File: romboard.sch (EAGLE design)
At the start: 13 parts

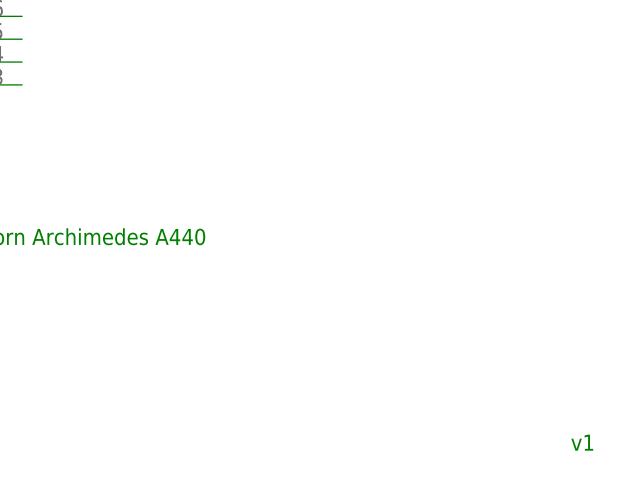
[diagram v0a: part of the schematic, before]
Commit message: Add licence to schematic, board
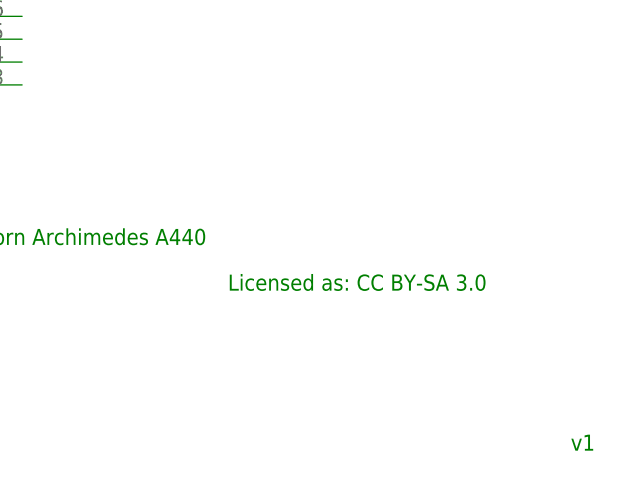
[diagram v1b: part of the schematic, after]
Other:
- note added: "Licensed as: CC BY-SA 3.0"
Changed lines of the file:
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@@
 <grid distance="0.1" unitdist="inch" unit="inch" style="lines" multiple="1" display="no" altdistance="0.01" altunitdist="inch" altunit="inch"/>
 <layers>
-<layer number="1" name="Top" color="4" fill="1" visible="yes" active="no"/>
-<layer number="16" name="Bottom" color="1" fill="1" visible="yes" active="no"/>
-<layer number="17" name="Pads" color="2" fill="1" visible="yes" active="no"/>
-<layer number="18" name="Vias" color="2" fill="1" visible="yes" active="no"/>
-<layer number="19" name="Unrouted" color="6" fill="1" visible="yes" active="no"/>
-<layer number="20" name="Dimension" color="15" fill="1" visible="yes" active="no"/>
-<layer number="21" name="tPlace" color="7" fill="1" visible="yes" active="no"/>
-<layer number="22" name="bPlace" color="7" fill="1" visible="yes" active="no"/>
-<layer number="23" name="tOrigins" color="15" fill="1" visible="yes" active="no"/>
-<layer number="24" name="bOrigins" color="15" fill="1" visible="yes" active="no"/>
-<layer number="25" name="tNames" color="7" fill="1" visible="yes" active="no"/>
-<layer number="26" name="bNames" color="7" fill="1" visible="yes" active="no"/>
-<layer number="27" name="tValues" color="7" fill="1" visible="yes" active="no"/>
-<layer number="28" name="bValues" color="7" fill="1" visible="yes" active="no"/>
+<layer number="1" name="Top" color="4" fill="1" visible="no" active="no"/>
+<layer number="16" name="Bottom" color="1" fill="1" visible="no" active="no"/>
+<layer number="17" name="Pads" color="2" fill="1" visible="no" active="no"/>
+<layer number="18" name="Vias" color="2" fill="1" visible="no" active="no"/>
+<layer number="19" name="Unrouted" color="6" fill="1" visible="no" active="no"/>
+<layer number="20" name="Dimension" color="15" fill="1" visible="no" active="no"/>
+<layer number="21" name="tPlace" color="7" fill="1" visible="no" active="no"/>
+<layer number="22" name="bPlace" color="7" fill="1" visible="no" active="no"/>
+<layer number="23" name="tOrigins" color="15" fill="1" visible="no" active="no"/>
+<layer number="24" name="bOrigins" color="15" fill="1" visible="no" active="no"/>
+<layer number="25" name="tNames" color="7" fill="1" visible="no" active="no"/>
+<layer number="26" name="bNames" color="7" fill="1" visible="no" active="no"/>
+<layer number="27" name="tValues" color="7" fill="1" visible="no" active="no"/>
+<layer number="28" name="bValues" color="7" fill="1" visible="no" active="no"/>
 <layer number="29" name="tStop" color="7" fill="3" visible="no" active="no"/>
 <layer number="30" name="bStop" color="7" fill="6" visible="no" active="no"/>
@@
 <layer number="35" name="tGlue" color="7" fill="4" visible="no" active="no"/>
 <layer number="36" name="bGlue" color="7" fill="5" visible="no" active="no"/>
-<layer number="37" name="tTest" color="7" fill="1" visible="yes" active="no"/>
-<layer number="38" name="bTest" color="7" fill="1" visible="yes" active="no"/>
+<layer number="37" name="tTest" color="7" fill="1" visible="no" active="no"/>
+<layer number="38" name="bTest" color="7" fill="1" visible="no" active="no"/>
 <layer number="39" name="tKeepout" color="4" fill="11" visible="no" active="no"/>
 <layer number="40" name="bKeepout" color="1" fill="11" visible="no" active="no"/>
@@
 <layer number="44" name="Drills" color="7" fill="1" visible="no" active="no"/>
 <layer number="45" name="Holes" color="7" fill="1" visible="no" active="no"/>
-<layer number="46" name="Milling" color="3" fill="1" visible="yes" active="no"/>
-<layer number="47" name="Measures" color="7" fill="1" visible="yes" active="no"/>
-<layer number="48" name="Document" color="7" fill="1" visible="yes" active="no"/>
-<layer number="49" name="Reference" color="7" fill="1" visible="yes" active="no"/>
+<layer number="46" name="Milling" color="3" fill="1" visible="no" active="no"/>
+<layer number="47" name="Measures" color="7" fill="1" visible="no" active="no"/>
+<layer number="48" name="Document" color="7" fill="1" visible="no" active="no"/>
+<layer number="49" name="Reference" color="7" fill="1" visible="no" active="no"/>
 <layer number="50" name="dxf" color="7" fill="1" visible="no" active="no"/>
-<layer number="51" name="tDocu" color="7" fill="1" visible="yes" active="no"/>
-<layer number="52" name="bDocu" color="7" fill="1" visible="yes" active="no"/>
+<layer number="51" name="tDocu" color="7" fill="1" visible="no" active="no"/>
+<layer number="52" name="bDocu" color="7" fill="1" visible="no" active="no"/>
 <layer number="53" name="tGND_GNDA" color="7" fill="9" visible="no" active="no"/>
 <layer number="54" name="bGND_GNDA" color="1" fill="9" visible="no" active="no"/>
@@
   JP1 2-3, JP2 1-2, 3-5, 4-6</text>
 <text x="266.7" y="7.62" size="1.778" layer="91">v1</text>
+<text x="228.6" y="25.4" size="1.778" layer="91">Licensed as: CC BY-SA 3.0</text>
 </plain>
 <instances>
